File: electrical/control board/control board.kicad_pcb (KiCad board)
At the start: 4 copper layers, 146.1 x 146.1 mm, 65 parts, among them J1 analog_extra, J2 Programming_Header, J3 Conn_01x08, J4 datamate_sensors, J5 datamate_motor, J6 datamate_misc, J7 48V_IN, J8 5V, P1 ODROID-C2, Q2 DTC114E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

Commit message: deleted previous board
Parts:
- removed C1: 0.1uF, Capacitor_SMD:C_0603_1608Metric_Pad1.05x0.95mm_HandSolder
- removed C10, C5, C6, C7, C8, C9: 100nF, Capacitor_SMD:C_0603_1608Metric_Pad1.05x0.95mm_HandSolder
- removed C11: C_Small, Capacitor_SMD:C_0603_1608Metric_Pad1.05x0.95mm_HandSolder
- removed C12, C13, C14, C22, C24, C4: 1uF, Capacitor_SMD:C_0603_1608Metric_Pad1.05x0.95mm_HandSolder
- removed C15, C17, C18, C23, C25: .1uF, Capacitor_SMD:C_0603_1608Metric_Pad1.05x0.95mm_HandSolder
- removed C16, C19: 10uF, Capacitor_SMD:C_0603_1608Metric_Pad1.05x0.95mm_HandSolder
- removed C2, C3: 30pF, Capacitor_SMD:C_0603_1608Metric_Pad1.05x0.95mm_HandSolder
- removed C20, C21: 4.7uF, Capacitor_SMD:C_0603_1608Metric_Pad1.05x0.95mm_HandSolder
- removed C26: 10pF, Capacitor_SMD:C_0603_1608Metric_Pad1.05x0.95mm_HandSolder
- removed C27: 2.2nF, Capacitor_SMD:C_0603_1608Metric_Pad1.05x0.95mm_HandSolder
- removed C28: 100pF, Capacitor_SMD:C_0603_1608Metric_Pad1.05x0.95mm_HandSolder
- removed C29, C30: 22uF, Capacitor_SMD:C_0603_1608Metric_Pad1.05x0.95mm_HandSolder
- removed G***: LOGO, footprints:goat_background
- removed J1: analog_extra, Connector_PinHeader_2.54mm:PinHeader_1x02_P2.54mm_Vertical
- removed J2: Programming_Header, Connector_PinHeader_2.54mm:PinHeader_1x06_P2.54mm_Vertical
- removed J3: Conn_01x08, Connector_PinHeader_2.54mm:PinHeader_1x08_P2.54mm_Vertical
- removed J4: datamate_sensors, Connector_PinHeader_2.54mm:PinHeader_1x04_P2.54mm_Vertical
- removed J5: datamate_motor, Connector_PinHeader_2.54mm:PinHeader_1x04_P2.54mm_Vertical
- removed J6: datamate_misc, Connector_PinHeader_2.54mm:PinHeader_1x04_P2.54mm_Vertical
- removed J7: 48V_IN, Connector_PinHeader_2.54mm:PinHeader_1x02_P2.54mm_Vertical
- removed J8: 5V, Connector_PinHeader_2.54mm:PinHeader_1x02_P2.54mm_Vertical
- removed L1, L2: 33uH, Inductor_THT:L_Radial_D12.0mm_P6.00mm_MuRATA_1900R
- removed P1: ODROID-C2, footprints:ODROID-C2
- removed Q2: DTC114E, Package_TO_SOT_SMD:SOT-23
- removed R1, R2: 4.7k, Resistor_SMD:R_0603_1608Metric_Pad1.05x0.95mm_HandSolder
- removed R13, R7: 10k, Resistor_SMD:R_0603_1608Metric_Pad1.05x0.95mm_HandSolder
- removed R14: 12k, Resistor_SMD:R_0603_1608Metric_Pad1.05x0.95mm_HandSolder
- removed R15, R23: 100k, Resistor_SMD:R_0603_1608Metric_Pad1.05x0.95mm_HandSolder
- removed R16: 3.6k, Resistor_SMD:R_0603_1608Metric_Pad1.05x0.95mm_HandSolder
- removed R24: 4.02k, Resistor_SMD:R_0603_1608Metric_Pad1.05x0.95mm_HandSolder
- removed R25: 5.11k, Resistor_SMD:R_0603_1608Metric_Pad1.05x0.95mm_HandSolder
- removed R6: 1m, footprints:FC4L64
- removed R8: 56k, Resistor_SMD:R_0603_1608Metric_Pad1.05x0.95mm_HandSolder
- removed U1: STM32F446RETx, Package_QFP:LQFP-64_10x10mm_P0.5mm
- removed U10, U9: LTC7103-LT7103, footprints:LTC7103
- removed U2: HIH6031, Package_SO:SOIC-8-N7_3.9x4.9mm_P1.27mm
- removed U3: INA240-INA240, Package_SO:TSSOP-8_4.4x3mm_P0.65mm
- removed U4, U5, U6: ADM3061, Package_SO:TSSOP-8_3x3mm_P0.65mm
- removed U7: ICM20648, footprints:ICM-20648
- removed U8: LD1117S33TR_SOT223, Package_TO_SOT_SMD:SOT-223-3_TabPin2
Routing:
- net +12V: track 343.8 -> 0.00 mm, vias 2 -> 0
- net +5V: track 161.4 -> 0.00 mm, vias 3 -> 0
- net /CURRENT_MEASURE: track 105.3 -> 0.00 mm, vias 5 -> 0
- net /SWDIO: track 100.4 -> 0.00 mm, vias 2 -> 0
- net GND: track 84.7 -> 0.00 mm, vias 70 -> 0
- net /JTDO: track 80.8 -> 0.00 mm
- net /SWCLK: track 78.5 -> 0.00 mm
- net /HIH_SDA: track 75.2 -> 0.00 mm, vias 3 -> 0
- net /NRST: track 73.5 -> 0.00 mm, vias 2 -> 0
- net /HIH_SCL: track 67.4 -> 0.00 mm, vias 1 -> 0
- net /48V_MEASURE: track 66.3 -> 0.00 mm, vias 3 -> 0
- net /ICM_SCL: track 65.2 -> 0.00 mm, vias 2 -> 0
- net /ICM_SDA: track 62.9 -> 0.00 mm, vias 2 -> 0
- net /SENSOR_RX: track 60.5 -> 0.00 mm, vias 1 -> 0
- net +3V3: track 59.5 -> 0.00 mm, vias 43 -> 0
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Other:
- board outline removed

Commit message: the correct board outline is now in the correct project
For real this time, I promise
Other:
- board outline added: 72.4 x 149.8 mm
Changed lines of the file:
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@@
   (general
     (thickness 1.6)
-    (drawings 0)
+    (drawings 2)
     (tracks 0)
     (zones 0)
@@
     (add_net GND)
   )
+  (gr_arc (start 105.664 94.190937) (end 103.124 19.304) (angle -176.1147961) (layer Edge.Cuts) (width 0.2))
+  (gr_line (start 103.124 19.304) (end 103.124 169.077874) (layer Edge.Cuts) (width 0.2))
   (zone (net 1) (net_name GND) (layer In1.Cu) (hatch edge 0.508)
     (connect_pads (clearance 0.508))

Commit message: some work on board
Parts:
- added C1: 0.1uF, Capacitor_SMD:C_0603_1608Metric_Pad1.05x0.95mm_HandSolder, F.Cu at (156.3, 29.3)
- added C10: 100nF, Capacitor_SMD:C_0603_1608Metric_Pad1.05x0.95mm_HandSolder, F.Cu at (153.0, 30.8)
- added C11: C_Small, Capacitor_SMD:C_0603_1608Metric_Pad1.05x0.95mm_HandSolder, F.Cu at (138.5, 44.2)
- added C13: 1uF, Capacitor_SMD:C_0603_1608Metric_Pad1.05x0.95mm_HandSolder, F.Cu at (147.8, 39.9)
- added C14: 1uF, Capacitor_SMD:C_0603_1608Metric_Pad1.05x0.95mm_HandSolder, F.Cu at (141.8, 44.2)
- added C15: .1uF, Capacitor_SMD:C_0603_1608Metric_Pad1.05x0.95mm_HandSolder, F.Cu at (159.7, 31.3)
- added C17: .1uF, Capacitor_SMD:C_0603_1608Metric_Pad1.05x0.95mm_HandSolder, F.Cu at (153.0, 32.3)
- added C18: .1uF, Capacitor_SMD:C_0603_1608Metric_Pad1.05x0.95mm_HandSolder, F.Cu at (148.8, 38.4)
- added C2: 30pF, Capacitor_SMD:C_0603_1608Metric_Pad1.05x0.95mm_HandSolder, F.Cu at (154.8, 36.8)
- added C3: 30pF, Capacitor_SMD:C_0603_1608Metric_Pad1.05x0.95mm_HandSolder, F.Cu at (159.7, 32.8)
- added C4: 1uF, Capacitor_SMD:C_0603_1608Metric_Pad1.05x0.95mm_HandSolder, F.Cu at (154.5, 39.8)
- added C5: 100nF, Capacitor_SMD:C_0603_1608Metric_Pad1.05x0.95mm_HandSolder, F.Cu at (159.7, 34.3)
- added C6: 100nF, Capacitor_SMD:C_0603_1608Metric_Pad1.05x0.95mm_HandSolder, F.Cu at (145.5, 38.4)
- added C7: 100nF, Capacitor_SMD:C_0603_1608Metric_Pad1.05x0.95mm_HandSolder, F.Cu at (148.5, 44.4)
- added C8: 100nF, Capacitor_SMD:C_0603_1608Metric_Pad1.05x0.95mm_HandSolder, F.Cu at (163.4, 28.3)
- added C9: 100nF, Capacitor_SMD:C_0603_1608Metric_Pad1.05x0.95mm_HandSolder, F.Cu at (153.0, 29.3)
- added J1: analog_extra, Connector_PinHeader_2.54mm:PinHeader_1x02_P2.54mm_Vertical, F.Cu at (96.5, 123.2)
- added J10: Motor_2, Connector_PinHeader_2.54mm:PinHeader_1x03_P2.54mm_Vertical, B.Cu at (82.3, 54.4)
- added J11: Motor_3, Connector_PinHeader_2.54mm:PinHeader_1x03_P2.54mm_Vertical, B.Cu at (78.2, 54.4)
- added J12: Motor_4, Connector_PinHeader_2.54mm:PinHeader_1x03_P2.54mm_Vertical, B.Cu at (74.2, 54.4)
- added J13: Motor_5, Connector_PinHeader_2.54mm:PinHeader_1x03_P2.54mm_Vertical, B.Cu at (70.1, 54.4)
- added J14: Motor_6, Connector_PinHeader_2.54mm:PinHeader_1x03_P2.54mm_Vertical, B.Cu at (66.5, 54.4)
- added J15: Motor_7, Connector_PinHeader_2.54mm:PinHeader_1x03_P2.54mm_Vertical, B.Cu at (63.2, 54.6)
- added J16: Motor_8, Connector_PinHeader_2.54mm:PinHeader_1x03_P2.54mm_Vertical, B.Cu at (59.2, 54.4)
- added J2: Programming_Header, Connector_PinHeader_2.54mm:PinHeader_1x06_P2.54mm_Vertical, F.Cu at (65.0, 99.1)
- added J3: Conn_01x08, Connector_PinHeader_2.54mm:PinHeader_1x08_P2.54mm_Vertical, F.Cu at (128.3, 15.7)
- added J4: datamate_sensors, Connector_PinHeader_2.54mm:PinHeader_1x04_P2.54mm_Vertical, F.Cu at (96.5, 39.9)
- added J5: Motor_1, Connector_PinHeader_2.54mm:PinHeader_1x03_P2.54mm_Vertical, B.Cu at (86.4, 54.4)
- added J6: datamate_misc, Connector_PinHeader_2.54mm:PinHeader_1x04_P2.54mm_Vertical, F.Cu at (96.3, 24.6)
- added P1: ODROID-C2, footprints:ODROID-C2, F.Cu at (98.8, 56.4)
- added Q2: DTC114E, Package_TO_SOT_SMD:SOT-23, F.Cu at (121.6, 43.0)
- added R1: 4.7k, Resistor_SMD:R_0603_1608Metric_Pad1.05x0.95mm_HandSolder, F.Cu at (156.3, 32.3)
- added R10: R_Small, Resistor_SMD:R_0603_1608Metric_Pad1.05x0.95mm_HandSolder, F.Cu at (163.0, 29.8)
- added R11: R_Small, Resistor_SMD:R_0603_1608Metric_Pad1.05x0.95mm_HandSolder, F.Cu at (151.1, 39.9)
- added R12: 10k, Resistor_SMD:R_0603_1608Metric_Pad1.05x0.95mm_HandSolder, F.Cu at (151.4, 35.3)
- added R13: 10k, Resistor_SMD:R_0603_1608Metric_Pad1.05x0.95mm_HandSolder, F.Cu at (156.3, 33.8)
- added R14: 12k, Resistor_SMD:R_0603_1608Metric_Pad1.05x0.95mm_HandSolder, F.Cu at (159.7, 29.8)
- added R15: 100k, Resistor_SMD:R_0603_1608Metric_Pad1.05x0.95mm_HandSolder, F.Cu at (147.8, 42.9)
- added R16: 3.6k, Resistor_SMD:R_0603_1608Metric_Pad1.05x0.95mm_HandSolder, F.Cu at (163.4, 26.8)
- added R17: R_Small, Resistor_SMD:R_0603_1608Metric_Pad1.05x0.95mm_HandSolder, F.Cu at (152.2, 38.3)
- added R18: R_Small, Resistor_SMD:R_0603_1608Metric_Pad1.05x0.95mm_HandSolder, F.Cu at (151.1, 41.4)
- added R19: R_Small, Resistor_SMD:R_0603_1608Metric_Pad1.05x0.95mm_HandSolder, F.Cu at (151.4, 36.8)
- added R2: 4.7k, Resistor_SMD:R_0603_1608Metric_Pad1.05x0.95mm_HandSolder, F.Cu at (160.1, 28.3)
- added R3: 10k, Resistor_SMD:R_0603_1608Metric_Pad1.05x0.95mm_HandSolder, F.Cu at (147.8, 41.4)
- added R4: 10k, Resistor_SMD:R_0603_1608Metric_Pad1.05x0.95mm_HandSolder, F.Cu at (160.1, 26.8)
- added R5: 10k, Resistor_SMD:R_0603_1608Metric_Pad1.05x0.95mm_HandSolder, F.Cu at (156.3, 30.8)
- added R6: 1m, footprints:FC4L64, F.Cu at (109.5, 145.1)
- added R7: 10k, Resistor_SMD:R_0603_1608Metric_Pad1.05x0.95mm_HandSolder, F.Cu at (153.0, 33.8)
- added R8: 56k, Resistor_SMD:R_0603_1608Metric_Pad1.05x0.95mm_HandSolder, F.Cu at (145.2, 44.4)
- added R9: R_Small, Resistor_SMD:R_0603_1608Metric_Pad1.05x0.95mm_HandSolder, F.Cu at (154.8, 35.3)
- added U1: STM32F446RETx, Package_QFP:LQFP-64_10x10mm_P0.5mm, B.Cu at (69.6, 80.0)
- added U2: HIH6031, Package_SO:SOIC-8-N7_3.9x4.9mm_P1.27mm, F.Cu at (147.5, 31.2)
- added U3: INA240-INA240, Package_SO:TSSOP-8_4.4x3mm_P0.65mm, F.Cu at (142.1, 41.6)
- added U4: ADM3061, Package_SO:TSSOP-8_3x3mm_P0.65mm, F.Cu at (146.8, 35.8)
- added U6: ADM3061, Package_SO:TSSOP-8_3x3mm_P0.65mm, F.Cu at (133.8, 43.3)
- added U7: ICM20648, footprints:ICM-20648, F.Cu at (112.4, 136.7)
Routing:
- added copper zone on F.Cu, net GND

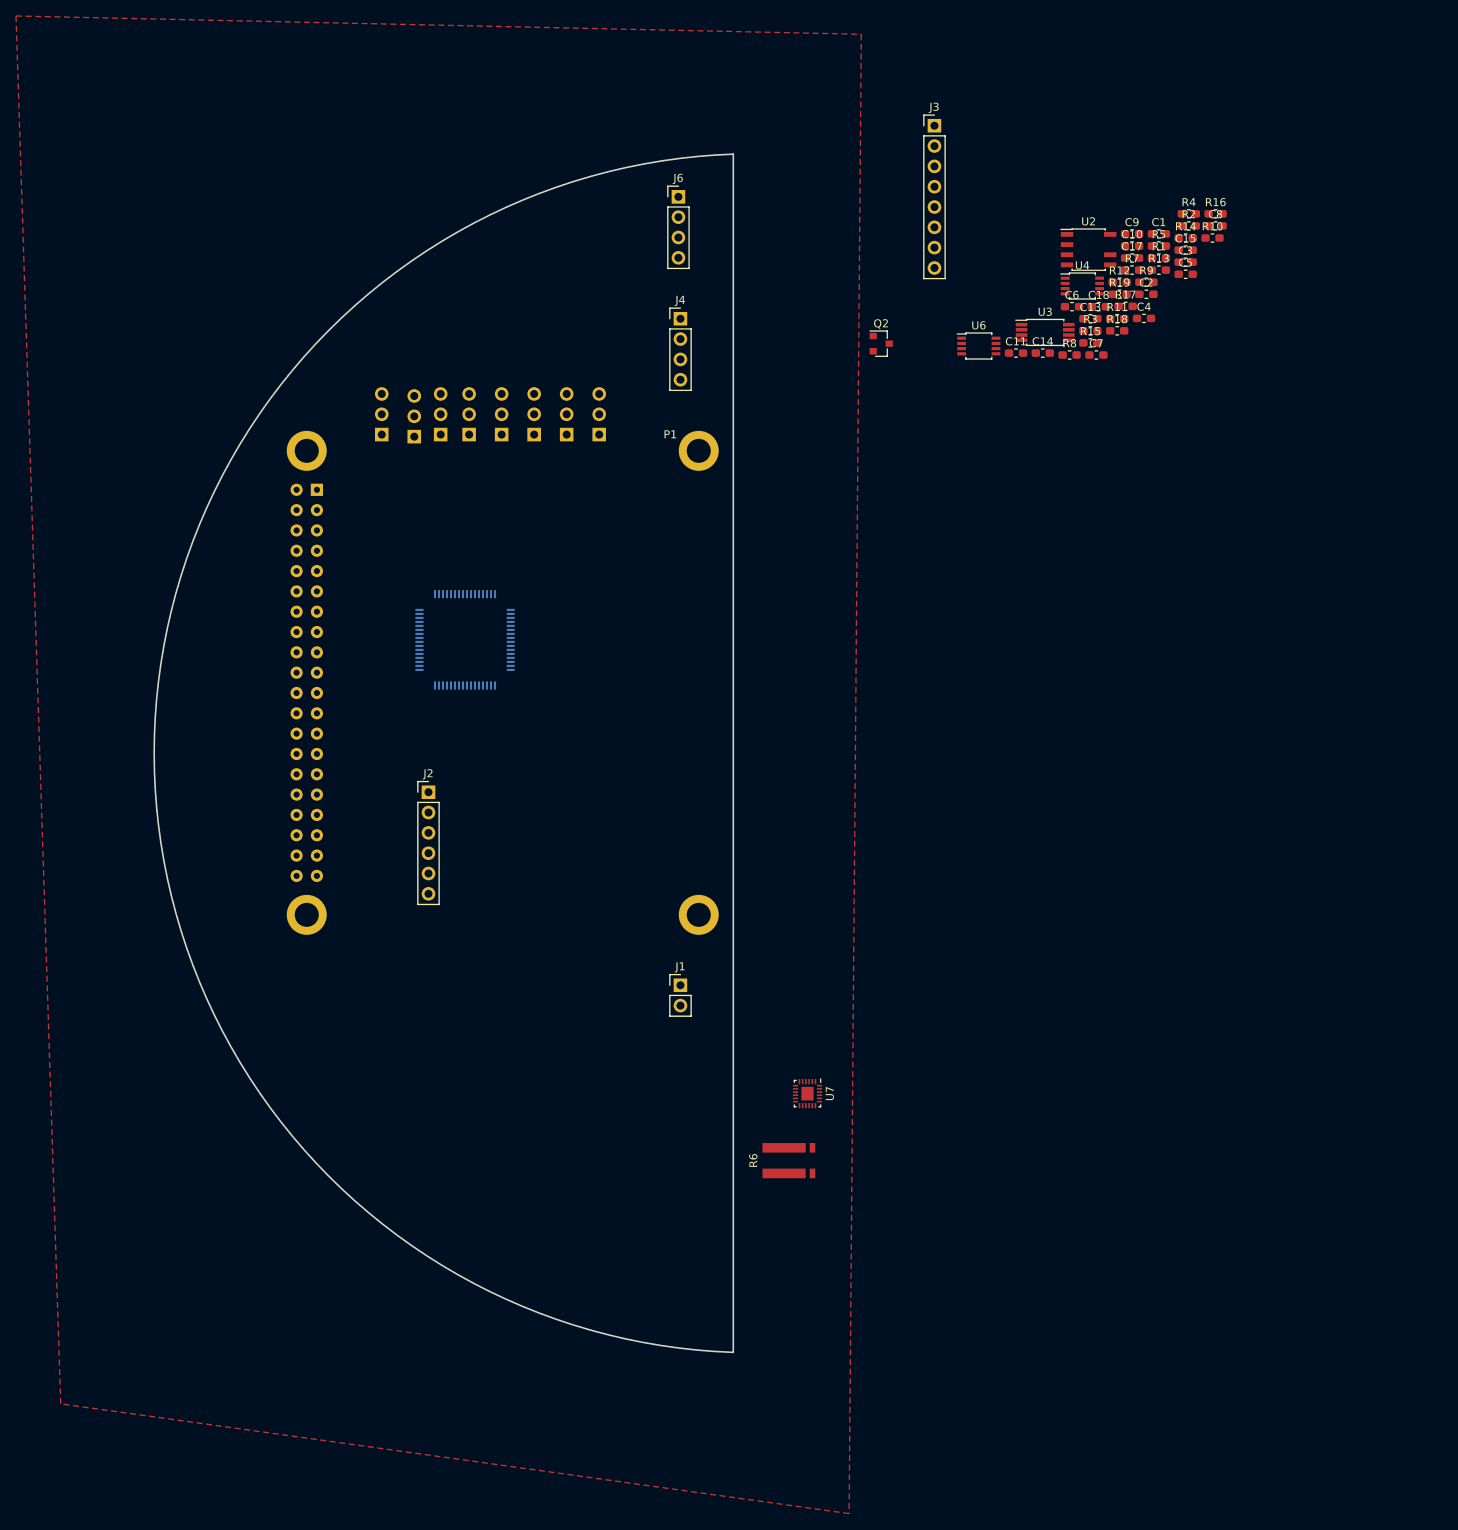
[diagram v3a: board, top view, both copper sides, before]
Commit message: Moved current measurement to power board
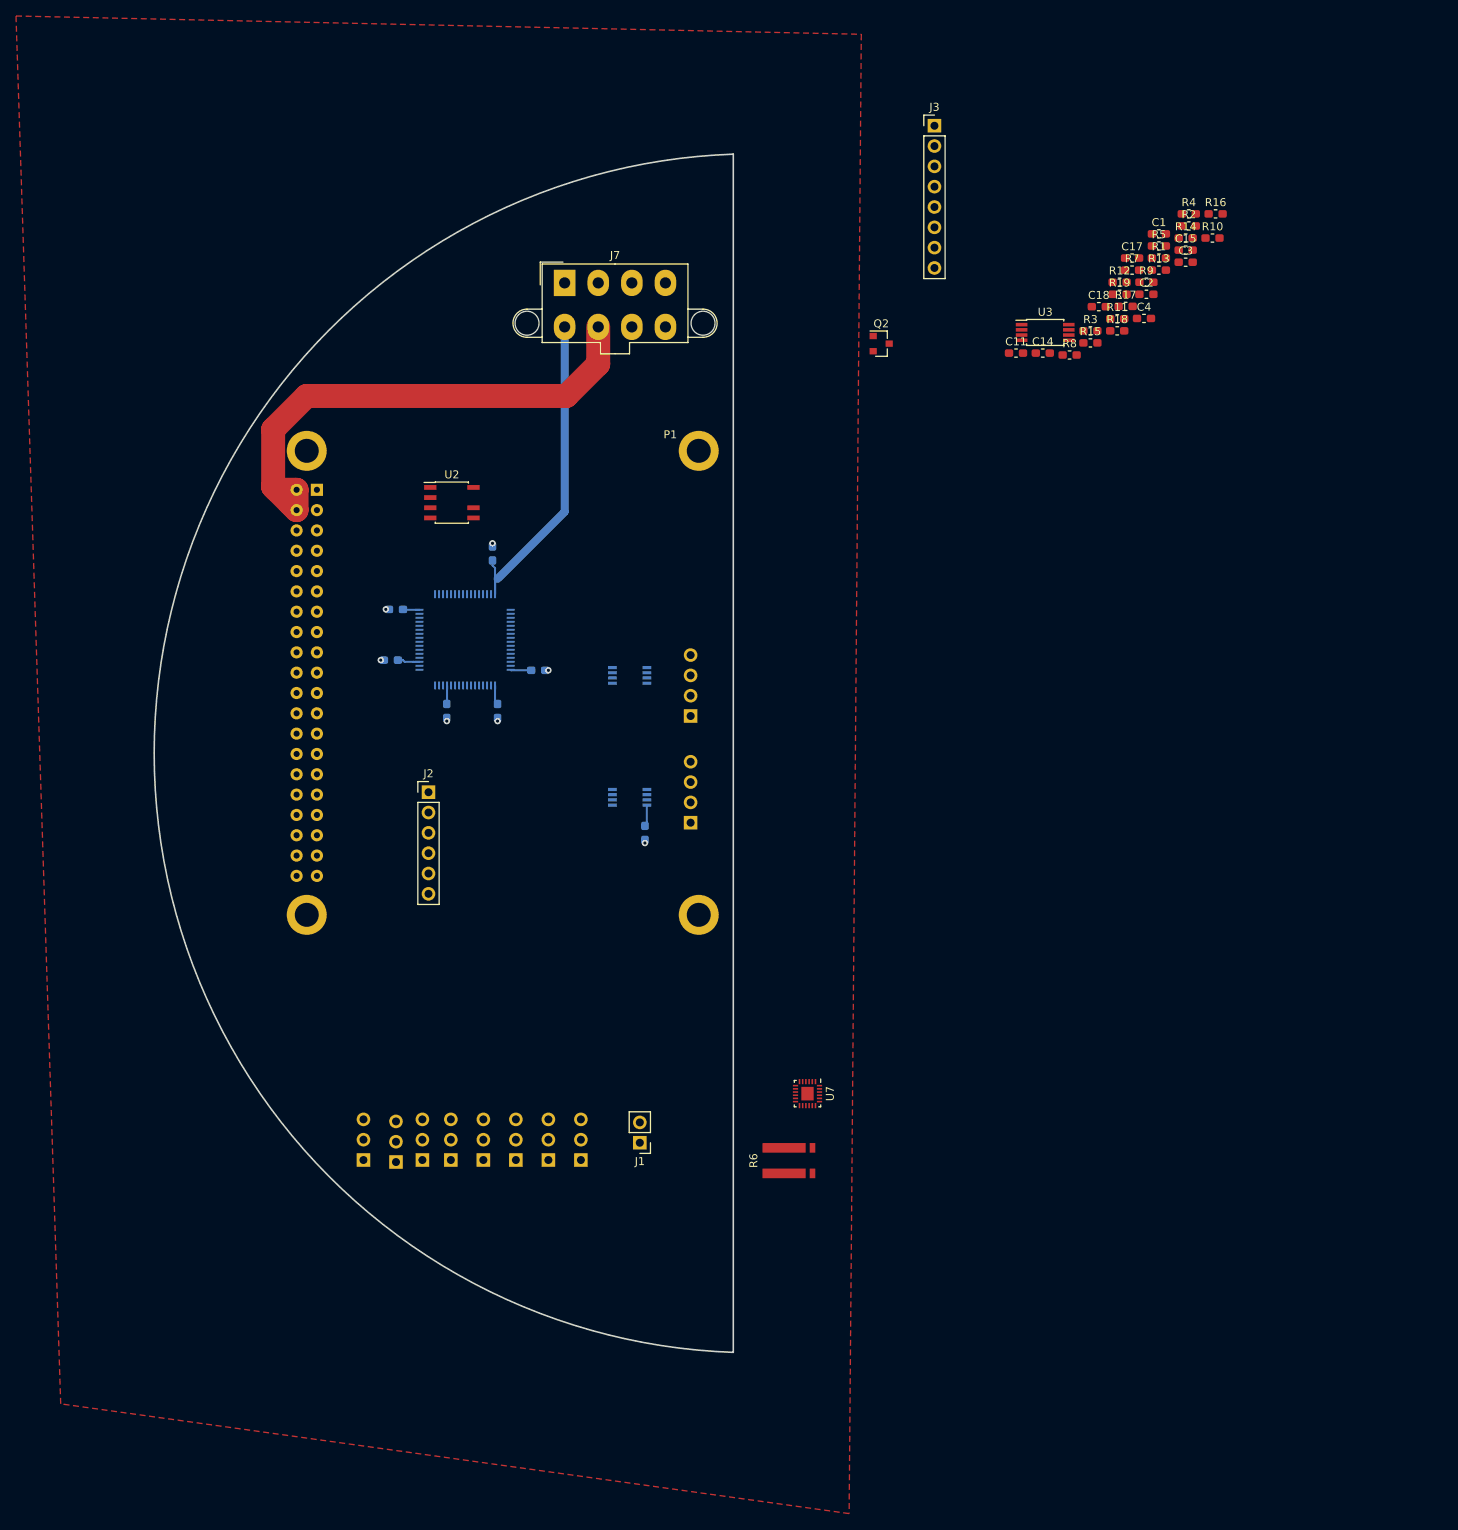
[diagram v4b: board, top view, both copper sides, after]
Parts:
- added J7: Power_Connector, Connector_Molex:Molex_Mini-Fit_Jr_5566-08A2_2x04_P4.20mm_Vertical, F.Cu at (82.0, 35.4)
- C10, C13, C5, C6, C7, C8, C9, J4, J6, U4, U6: moved to B.Cu
- moved C8 113.6 mm to (67.3, 88.9), turned to 90 degrees
- moved C9 99.2 mm to (73.7, 88.9), turned to 90 degrees
- moved C7 96.1 mm to (60.3, 82.5)
- moved C5 93.4 mm to (73.0, 69.2), turned to 270 degrees
- moved C6 92.6 mm to (61.0, 76.2)
- moved C10 91.2 mm to (78.7, 83.8), turned to 180 degrees
- moved J15 90.7 mm to (61.0, 145.3)
- moved J10 90.7 mm to (80.0, 145.0)
- moved J11 90.7 mm to (75.9, 145.0)
- moved J12 90.7 mm to (71.9, 145.0)
- moved J13 90.7 mm to (67.8, 145.0)
- moved J14 90.7 mm to (64.3, 145.0)
- moved J16 90.7 mm to (56.9, 145.0)
- moved J5 90.7 mm to (84.1, 145.0)
- moved U2 85.7 mm to (67.9, 62.9)
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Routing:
- net +5V: track 0.00 -> 65.6 mm
- net +3V3: track 0.00 -> 56.3 mm
- net GND: vias 0 -> 7

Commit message: forgot to remove current measurement from pcb
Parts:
- removed C11: C_Small, Capacitor_SMD:C_0603_1608Metric_Pad1.05x0.95mm_HandSolder
- removed R6: 1m, footprints:FC4L64
- removed U3: INA240-INA240, Package_SO:TSSOP-8_4.4x3mm_P0.65mm
- moved U7 23.1 mm to (93.3, 149.9)
